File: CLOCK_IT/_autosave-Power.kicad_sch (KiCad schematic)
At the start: 50 parts, among them Q1 AO3400A, Q2 AO3400A, SW1 CK_KMS2xxG, U10 DS1307ZN_, U4 AXP2101, U5 MC-264, Y2 ABS07-32.768KHZ-T

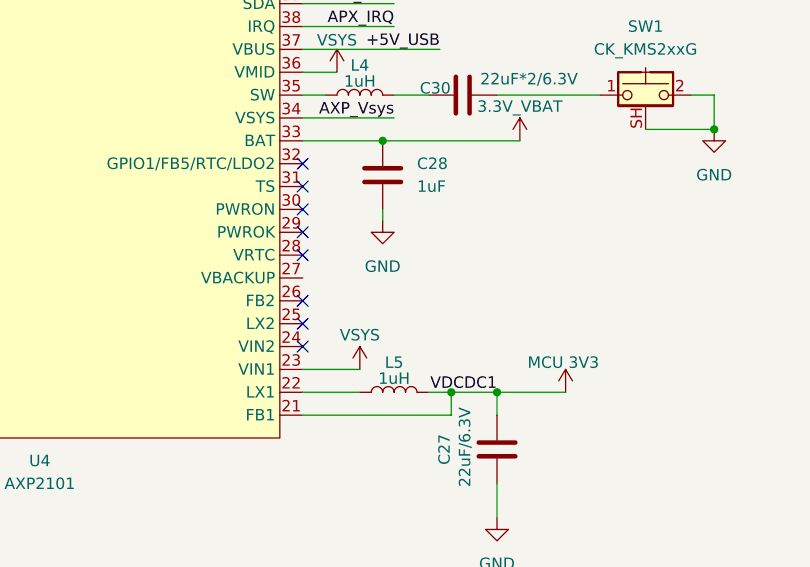
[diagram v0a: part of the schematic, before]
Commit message: :art: small Rereading errors for axp21010
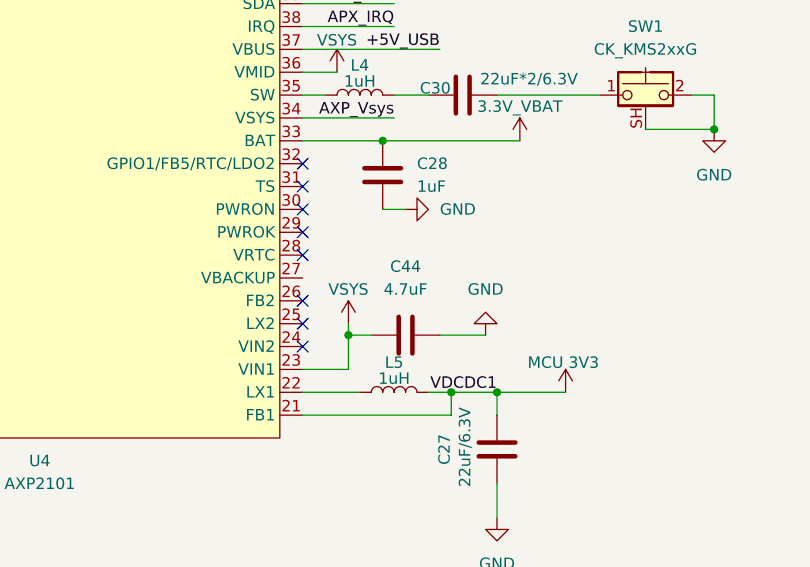
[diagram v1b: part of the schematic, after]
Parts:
- added C44: 4.7uF, symbol Device:C
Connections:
- net GND: now also C44.2
- net VSYS: now also C44.1
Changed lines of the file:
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@@
 	)
 	(junction
+		(at 201.93 78.74)
+		(diameter 0)
+		(color 0 0 0 0)
+	)
+	(junction
 		(at 289.56 58.42)
 		(diameter 0)
@@
 	(wire
 		(pts
+			(xy 201.93 77.47) (xy 201.93 78.74)
+		)
+		(stroke
+			(width 0)
+			(type default)
+		)
+	)
+	(wire
+		(pts
 			(xy 115.57 201.93) (xy 120.65 201.93)
 		)
@@
 	(wire
 		(pts
-			(xy 205.74 64.77) (xy 205.74 66.04)
+			(xy 234.95 55.88) (xy 242.57 55.88)
 		)
 		(stroke
@@
 	(wire
 		(pts
-			(xy 234.95 55.88) (xy 242.57 55.88)
+			(xy 306.07 62.23) (xy 306.07 58.42)
 		)
 		(stroke
@@
 	(wire
 		(pts
-			(xy 306.07 62.23) (xy 306.07 58.42)
+			(xy 124.46 87.63) (xy 133.35 87.63)
 		)
 		(stroke
@@
 	(wire
 		(pts
-			(xy 124.46 87.63) (xy 133.35 87.63)
+			(xy 121.92 52.07) (xy 135.89 52.07)
 		)
 		(stroke
@@
 	(wire
 		(pts
-			(xy 121.92 52.07) (xy 135.89 52.07)
+			(xy 134.62 49.53) (xy 138.43 49.53)
 		)
 		(stroke
@@
 	(wire
 		(pts
-			(xy 134.62 49.53) (xy 138.43 49.53)
+			(xy 201.93 78.74) (xy 204.47 78.74)
 		)
 		(stroke
@@
 	(wire
 		(pts
+			(xy 201.93 78.74) (xy 201.93 82.55)
+		)
+		(stroke
+			(width 0)
+			(type default)
+		)
+	)
+	(wire
+		(pts
 			(xy 138.43 44.45) (xy 120.65 44.45)
 		)
@@
 	(wire
 		(pts
+			(xy 212.09 78.74) (xy 217.17 78.74)
+		)
+		(stroke
+			(width 0)
+			(type default)
+		)
+	)
+	(wire
+		(pts
 			(xy 119.38 38.1) (xy 119.38 35.56)
 		)
@@
 	(wire
 		(pts
+			(xy 208.28 64.77) (xy 205.74 64.77)
+		)
+		(stroke
+			(width 0)
+			(type default)
+		)
+	)
+	(wire
+		(pts
 			(xy 288.29 43.18) (xy 297.18 43.18)
 		)
@@
 	(wire
 		(pts
+			(xy 201.93 82.55) (xy 196.85 82.55)
+		)
+		(stroke
+			(width 0)
+			(type default)
+		)
+	)
+	(wire
+		(pts
 			(xy 35.56 40.64) (xy 35.56 45.72)
 		)
@@
 	(wire
 		(pts
-			(xy 196.85 82.55) (xy 203.2 82.55)
-		)
-		(stroke
-			(width 0)
-			(type default)
-		)
-	)
-	(wire
-		(pts
 			(xy 289.56 68.58) (xy 289.56 58.42)
 		)
@@
 	(symbol
 		(lib_id "power:GND")
-		(at 205.74 66.04 0)
+		(at 208.28 64.77 90)
 		(unit 1)
 		(exclude_from_sim no)
@@
 		(fields_autoplaced yes)
 		(property "Reference" "#PWR071"
-			(at 205.74 72.39 0)
+			(at 214.63 64.77 0)
 			(effects
 				(font
@@
 		)
 		(property "Value" "GND"
-			(at 205.74 71.12 0)
+			(at 212.09 64.7699 90)
 			(effects
 				(font
 					(size 1.27 1.27)
 				)
+				(justify right)
 			)
 		)
 		(property "Footprint" ""
-			(at 205.74 66.04 0)
+			(at 208.28 64.77 0)
 			(effects
 				(font
@@
 		)
 		(property "Datasheet" ""
-			(at 205.74 66.04 0)
+			(at 208.28 64.77 0)
 			(effects
 				(font
@@
 		)
 		(property "Description" "Power symbol creates a global label with name \"GND\" , ground"
-			(at 205.74 66.04 0)
+			(at 208.28 64.77 0)
 			(effects
 				(font
@@
 	(symbol
 		(lib_id "power:+3.3V")
-		(at 203.2 82.55 0)
+		(at 201.93 77.47 0)
 		(unit 1)
 		(exclude_from_sim no)
@@
 		(dnp no)
 		(property "Reference" "#PWR047"
-			(at 203.2 86.36 0)
+			(at 201.93 81.28 0)
 			(effects
 				(font
@@
 		)
 		(property "Value" "VSYS"
-			(at 203.2 78.74 0)
+			(at 201.93 73.66 0)
 			(effects
 				(font
@@
 		)
 		(property "Footprint" ""
-			(at 203.2 82.55 0)
+			(at 201.93 77.47 0)
 			(effects
 				(font
@@
 		)
 		(property "Datasheet" ""
-			(at 203.2 82.55 0)
+			(at 201.93 77.47 0)
 			(effects
 				(font
@@
 		)
 		(property "Description" "Power symbol creates a global label with name \"+3.3V\""
-			(at 203.2 82.55 0)
+			(at 201.93 77.47 0)
 			(effects
 				(font
@@
 	)
 	(symbol
+		(lib_id "Device:C")
+		(at 208.28 78.74 90)
+		(unit 1)
+		(exclude_from_sim no)
+		(in_bom yes)
+		(on_board yes)
+		(dnp no)
+		(fields_autoplaced yes)
+		(property "Reference" "C44"
+			(at 208.28 71.12 90)
+			(effects
+				(font
+					(size 1.27 1.27)
+				)
+			)
+		)
+		(property "Value" "4.7uF"
+			(at 208.28 73.66 90)
+			(effects
+				(font
+					(size 1.27 1.27)
+				)
+			)
+		)
+		(property "Footprint" ""
+			(at 212.09 77.7748 0)
+			(effects
+				(font
+					(size 1.27 1.27)
+				)
+				(hide yes)
+			)
+		)
+		(property "Datasheet" "~"
+			(at 208.28 78.74 0)
+			(effects
+				(font
+					(size 1.27 1.27)
+				)
+				(hide yes)
+			)
+		)
+		(property "Description" "Unpolarized capacitor"
+			(at 208.28 78.74 0)
+			(effects
+				(font
+					(size 1.27 1.27)
+				)
+				(hide yes)
+			)
+		)
+		(pin "2"
+		)
+		(pin "1"
+		)
+		(instances
+			(project "CLOCK_IT"
+				(path "/6c8f4e2a-0be1-4eb1-92e1-07339040f4c9/89057fe9-a1d2-4b06-95ab-71c40c05c07f"
+					(reference "C44")
+					(unit 1)
+				)
+			)
+		)
+	)
+	(symbol
 		(lib_id "Device:R")
 		(at 297.18 35.56 180)
@@
 					(unit 1)
 				)
+			)
+		)
+	)
+	(symbol
+		(lib_id "power:GND")
+		(at 217.17 78.74 180)
+		(unit 1)
+		(exclude_from_sim no)
+		(in_bom yes)
+		(on_board yes)
+		(dnp no)
+		(fields_autoplaced yes)
+		(property "Reference" "#PWR077"
+			(at 217.17 72.39 0)
+			(effects
+				(font
+					(size 1.27 1.27)
+				)
+				(hide yes)
+			)
+		)
+		(property "Value" "GND"
+			(at 217.17 73.66 0)
+			(effects
+				(font
+					(size 1.27 1.27)
+				)
+			)
+		)
+		(property "Footprint" ""
+			(at 217.17 78.74 0)
+			(effects
+				(font
+					(size 1.27 1.27)
+				)
+				(hide yes)
+			)
+		)
+		(property "Datasheet" ""
+			(at 217.17 78.74 0)
+			(effects
+				(font
+					(size 1.27 1.27)
+				)
+				(hide yes)
+			)
+		)
+		(property "Description" "Power symbol creates a global label with name \"GND\" , ground"
+			(at 217.17 78.74 0)
+			(effects
+				(font
+					(size 1.27 1.27)
+				)
+				(hide yes)
+			)
+		)
+		(pin "1"
+		)
+		(instances
+			(project "CLOCK_IT"
+				(path "/6c8f4e2a-0be1-4eb1-92e1-07339040f4c9/89057fe9-a1d2-4b06-95ab-71c40c05c07f"
+					(reference "#PWR077")
+					(unit 1)
+				)
